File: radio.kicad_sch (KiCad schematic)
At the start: 17 parts, among them U8 Si4468/7, Y2 26MHz

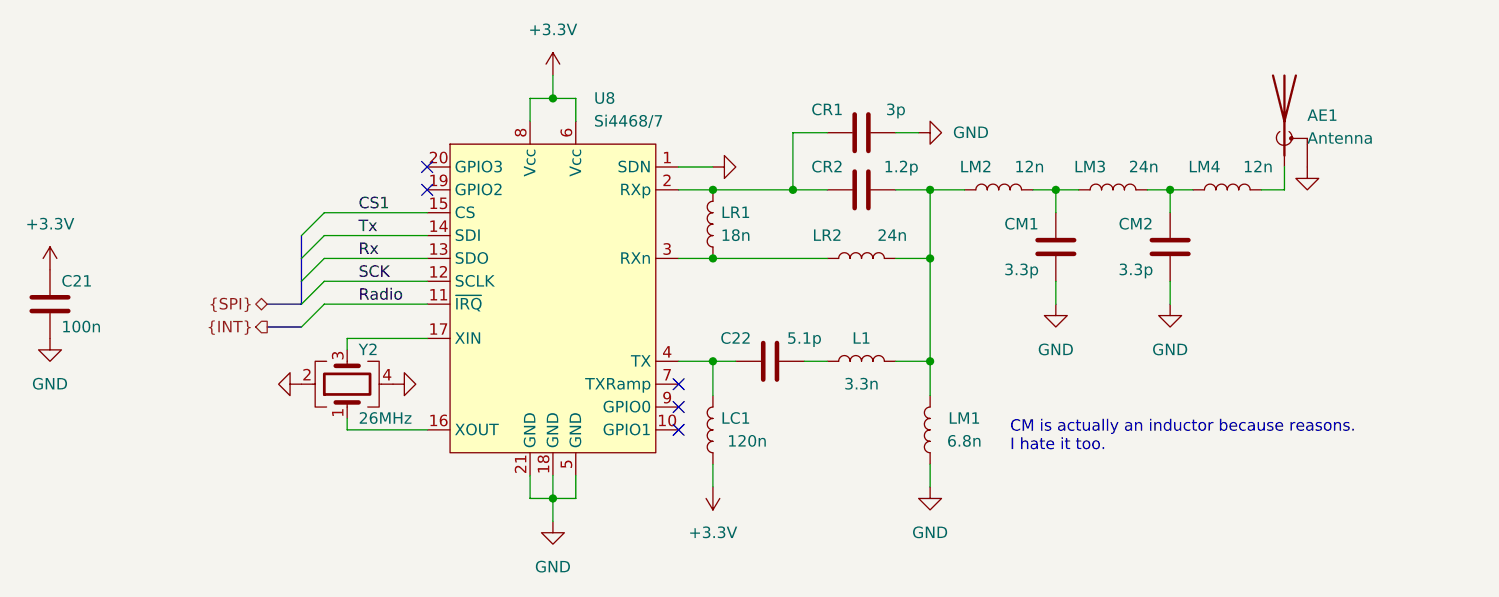
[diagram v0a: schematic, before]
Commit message: Geographical reannotated
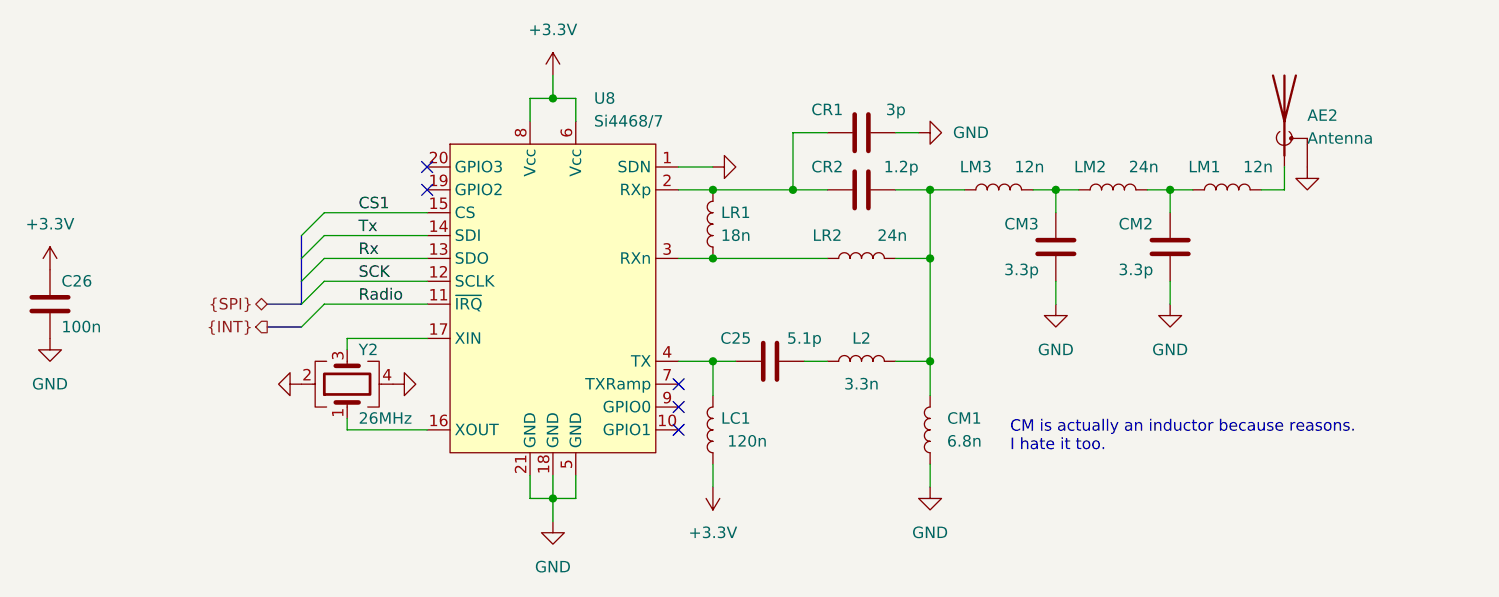
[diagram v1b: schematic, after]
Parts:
- renumbered AE1 to AE2, C22 to C25, C21 to C26, LM1 to CM1, CM1 to CM3, L1 to L2, LM4 to LM1, LM3 to LM2, LM2 to LM3
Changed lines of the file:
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@@
   (symbol (lib_id "Device:Antenna_Shield") (at 163.83 44.45 0) (unit 1)
     (in_bom yes) (on_board yes) (fields_autoplaced)
-    (property "Reference" "AE1" (id 0) (at 166.37 43.8149 0)
+    (property "Reference" "AE2" (id 0) (at 166.37 43.8149 0)
       (effects (font (size 1.27 1.27)) (justify left))
     )
@@
   (symbol (lib_id "Device:L") (at 144.78 52.07 270) (mirror x) (unit 1)
     (in_bom yes) (on_board yes)
-    (property "Reference" "LM3" (id 0) (at 142.24 49.53 90))
+    (property "Reference" "LM2" (id 0) (at 142.24 49.53 90))
     (property "Value" "24n" (id 1) (at 149.86 49.53 90)
       (effects (font (size 1.27 1.27)) (justify right))
@@
   (symbol (lib_id "Device:L") (at 116.84 71.12 90) (unit 1)
     (in_bom yes) (on_board yes)
-    (property "Reference" "L1" (id 0) (at 116.84 68.58 90))
+    (property "Reference" "L2" (id 0) (at 116.84 68.58 90))
     (property "Value" "3.3n" (id 1) (at 116.84 73.66 90))
     (property "Footprint" "Inductor_SMD:L_0603_1608Metric" (id 2) (at 116.84 71.12 0)
@@
   (symbol (lib_id "Device:L") (at 157.48 52.07 270) (mirror x) (unit 1)
     (in_bom yes) (on_board yes)
-    (property "Reference" "LM4" (id 0) (at 154.94 49.53 90))
+    (property "Reference" "LM1" (id 0) (at 154.94 49.53 90))
     (property "Value" "12n" (id 1) (at 162.56 49.53 90)
       (effects (font (size 1.27 1.27)) (justify right))
@@
   (symbol (lib_id "Device:C") (at 106.68 71.12 270) (mirror x) (unit 1)
     (in_bom yes) (on_board yes)
-    (property "Reference" "C22" (id 0) (at 102.87 68.58 90))
+    (property "Reference" "C25" (id 0) (at 102.87 68.58 90))
     (property "Value" "5.1p" (id 1) (at 110.49 68.58 90))
     (property "Footprint" "Capacitor_SMD:C_0603_1608Metric" (id 2) (at 102.87 70.1548 0)
@@
   (symbol (lib_id "Device:L") (at 124.46 78.74 180) (unit 1)
     (in_bom yes) (on_board yes)
-    (property "Reference" "LM1" (id 0) (at 128.27 77.47 0))
+    (property "Reference" "CM1" (id 0) (at 128.27 77.47 0))
     (property "Value" "6.8n" (id 1) (at 128.27 80.01 0))
     (property "Footprint" "Capacitor_SMD:C_0603_1608Metric" (id 2) (at 124.46 78.74 0)
@@
   (symbol (lib_id "Device:L") (at 132.08 52.07 270) (mirror x) (unit 1)
     (in_bom yes) (on_board yes)
-    (property "Reference" "LM2" (id 0) (at 129.54 49.53 90))
+    (property "Reference" "LM3" (id 0) (at 129.54 49.53 90))
     (property "Value" "12n" (id 1) (at 137.16 49.53 90)
       (effects (font (size 1.27 1.27)) (justify right))
@@
   (symbol (lib_id "Device:C") (at 138.43 58.42 0) (mirror y) (unit 1)
     (in_bom yes) (on_board yes)
-    (property "Reference" "CM1" (id 0) (at 134.62 55.88 0))
+    (property "Reference" "CM3" (id 0) (at 134.62 55.88 0))
     (property "Value" "3.3p" (id 1) (at 134.62 60.96 0))
     (property "Footprint" "Capacitor_SMD:C_0603_1608Metric" (id 2) (at 137.4648 62.23 0)
@@
   (symbol (lib_id "Device:C") (at 26.67 64.77 0) (unit 1)
     (in_bom yes) (on_board yes)
-    (property "Reference" "C21" (id 0) (at 27.94 62.23 0)
-      (effects (font (size 1.27 1.27)) (justify left))
-    )
+    (property "Reference" "C26" (id 0) (at 27.94 62.23 0)
+      (effects (font (size 1.27 1.27)) (justify left))
+    )

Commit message: Final refinements before issue to JLC
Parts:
- renumbered AE2 to AE1, C26 to C21, C25 to C22, CM3 to CM2, CM2 to CM3, L2 to L1, LM3 to LM1, LM1 to LM3
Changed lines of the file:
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@@
   (symbol (lib_id "Device:Antenna_Shield") (at 163.83 44.45 0) (unit 1)
     (in_bom yes) (on_board yes) (fields_autoplaced)
-    (property "Reference" "AE2" (id 0) (at 166.37 43.8149 0)
+    (property "Reference" "AE1" (id 0) (at 166.37 43.8149 0)
       (effects (font (size 1.27 1.27)) (justify left))
     )
@@
   (symbol (lib_id "power:GND") (at 100.33 49.53 90) (unit 1)
     (in_bom yes) (on_board yes) (fields_autoplaced)
-    (property "Reference" "#PWR053" (id 0) (at 106.68 49.53 0)
+    (property "Reference" "#PWR055" (id 0) (at 106.68 49.53 0)
       (effects (font (size 1.27 1.27)) hide)
     )
@@
   (symbol (lib_id "power:GND") (at 54.61 73.66 270) (unit 1)
     (in_bom yes) (on_board yes) (fields_autoplaced)
-    (property "Reference" "#PWR049" (id 0) (at 48.26 73.66 0)
+    (property "Reference" "#PWR051" (id 0) (at 48.26 73.66 0)
       (effects (font (size 1.27 1.27)) hide)
     )
@@
   (symbol (lib_id "power:GND") (at 166.37 49.53 0) (unit 1)
     (in_bom yes) (on_board yes) (fields_autoplaced)
-    (property "Reference" "#PWR059" (id 0) (at 166.37 55.88 0)
+    (property "Reference" "#PWR061" (id 0) (at 166.37 55.88 0)
       (effects (font (size 1.27 1.27)) hide)
     )
@@
   (symbol (lib_id "Device:L") (at 116.84 71.12 90) (unit 1)
     (in_bom yes) (on_board yes)
-    (property "Reference" "L2" (id 0) (at 116.84 68.58 90))
+    (property "Reference" "L1" (id 0) (at 116.84 68.58 90))
     (property "Value" "3.3n" (id 1) (at 116.84 73.66 90))
     (property "Footprint" "Inductor_SMD:L_0603_1608Metric" (id 2) (at 116.84 71.12 0)
@@
   (symbol (lib_id "power:GND") (at 151.13 64.77 0) (unit 1)
     (in_bom yes) (on_board yes) (fields_autoplaced)
-    (property "Reference" "#PWR058" (id 0) (at 151.13 71.12 0)
+    (property "Reference" "#PWR060" (id 0) (at 151.13 71.12 0)
       (effects (font (size 1.27 1.27)) hide)
     )
@@
   (symbol (lib_id "Device:L") (at 157.48 52.07 270) (mirror x) (unit 1)
     (in_bom yes) (on_board yes)
-    (property "Reference" "LM1" (id 0) (at 154.94 49.53 90))
+    (property "Reference" "LM3" (id 0) (at 154.94 49.53 90))
     (property "Value" "12n" (id 1) (at 162.56 49.53 90)
       (effects (font (size 1.27 1.27)) (justify right))
@@
   (symbol (lib_id "Device:C") (at 106.68 71.12 270) (mirror x) (unit 1)
     (in_bom yes) (on_board yes)
-    (property "Reference" "C25" (id 0) (at 102.87 68.58 90))
+    (property "Reference" "C22" (id 0) (at 102.87 68.58 90))
     (property "Value" "5.1p" (id 1) (at 110.49 68.58 90))
     (property "Footprint" "Capacitor_SMD:C_0603_1608Metric" (id 2) (at 102.87 70.1548 0)
@@
   (symbol (lib_id "power:GND") (at 64.77 73.66 90) (unit 1)
     (in_bom yes) (on_board yes) (fields_autoplaced)
-    (property "Reference" "#PWR050" (id 0) (at 71.12 73.66 0)
+    (property "Reference" "#PWR052" (id 0) (at 71.12 73.66 0)
       (effects (font (size 1.27 1.27)) hide)
     )
@@
   (symbol (lib_id "power:GND") (at 138.43 64.77 0) (unit 1)
     (in_bom yes) (on_board yes) (fields_autoplaced)
-    (property "Reference" "#PWR057" (id 0) (at 138.43 71.12 0)
+    (property "Reference" "#PWR059" (id 0) (at 138.43 71.12 0)
       (effects (font (size 1.27 1.27)) hide)
     )
@@
   (symbol (lib_id "power:+3.3V") (at 82.55 39.37 0) (unit 1)
     (in_bom yes) (on_board yes) (fields_autoplaced)
-    (property "Reference" "#PWR051" (id 0) (at 82.55 43.18 0)
+    (property "Reference" "#PWR053" (id 0) (at 82.55 43.18 0)
       (effects (font (size 1.27 1.27)) hide)
     )
@@
   (symbol (lib_id "power:GND") (at 26.67 68.58 0) (unit 1)
     (in_bom yes) (on_board yes) (fields_autoplaced)
-    (property "Reference" "#PWR048" (id 0) (at 26.67 74.93 0)
+    (property "Reference" "#PWR050" (id 0) (at 26.67 74.93 0)
       (effects (font (size 1.27 1.27)) hide)
     )
@@
   (symbol (lib_id "Device:L") (at 132.08 52.07 270) (mirror x) (unit 1)
     (in_bom yes) (on_board yes)
-    (property "Reference" "LM3" (id 0) (at 129.54 49.53 90))
+    (property "Reference" "LM1" (id 0) (at 129.54 49.53 90))
     (property "Value" "12n" (id 1) (at 137.16 49.53 90)
       (effects (font (size 1.27 1.27)) (justify right))
@@
   (symbol (lib_id "Device:C") (at 138.43 58.42 0) (mirror y) (unit 1)
     (in_bom yes) (on_board yes)
-    (property "Reference" "CM3" (id 0) (at 134.62 55.88 0))
+    (property "Reference" "CM2" (id 0) (at 134.62 55.88 0))
     (property "Value" "3.3p" (id 1) (at 134.62 60.96 0))
     (property "Footprint" "Capacitor_SMD:C_0603_1608Metric" (id 2) (at 137.4648 62.23 0)
@@
   (symbol (lib_id "power:GND") (at 123.19 45.72 90) (unit 1)
     (in_bom yes) (on_board yes) (fields_autoplaced)
-    (property "Reference" "#PWR055" (id 0) (at 129.54 45.72 0)
+    (property "Reference" "#PWR057" (id 0) (at 129.54 45.72 0)
       (effects (font (size 1.27 1.27)) hide)
     )
@@
   (symbol (lib_id "power:GND") (at 124.46 85.09 0) (unit 1)
     (in_bom yes) (on_board yes) (fields_autoplaced)
-    (property "Reference" "#PWR056" (id 0) (at 124.46 91.44 0)
+    (property "Reference" "#PWR058" (id 0) (at 124.46 91.44 0)
       (effects (font (size 1.27 1.27)) hide)
     )
@@
   (symbol (lib_id "Device:C") (at 151.13 58.42 0) (mirror y) (unit 1)
     (in_bom yes) (on_board yes)
-    (property "Reference" "CM2" (id 0) (at 147.32 55.88 0))
+    (property "Reference" "CM3" (id 0) (at 147.32 55.88 0))
     (property "Value" "3.3p" (id 1) (at 147.32 60.96 0))
     (property "Footprint" "Capacitor_SMD:C_0603_1608Metric" (id 2) (at 150.1648 62.23 0)
@@
   (symbol (lib_id "power:+3.3V") (at 100.33 85.09 180) (unit 1)
     (in_bom yes) (on_board yes) (fields_autoplaced)
-    (property "Reference" "#PWR054" (id 0) (at 100.33 81.28 0)
+    (property "Reference" "#PWR056" (id 0) (at 100.33 81.28 0)
       (effects (font (size 1.27 1.27)) hide)
     )
@@
   (symbol (lib_id "power:GND") (at 82.55 88.9 0) (unit 1)
     (in_bom yes) (on_board yes) (fields_autoplaced)
-    (property "Reference" "#PWR052" (id 0) (at 82.55 95.25 0)
+    (property "Reference" "#PWR054" (id 0) (at 82.55 95.25 0)
       (effects (font (size 1.27 1.27)) hide)
     )
@@
   (symbol (lib_id "power:+3.3V") (at 26.67 60.96 0) (unit 1)
     (in_bom yes) (on_board yes) (fields_autoplaced)
-    (property "Reference" "#PWR047" (id 0) (at 26.67 64.77 0)
+    (property "Reference" "#PWR049" (id 0) (at 26.67 64.77 0)
       (effects (font (size 1.27 1.27)) hide)
     )
@@
   (symbol (lib_id "Device:C") (at 26.67 64.77 0) (unit 1)
     (in_bom yes) (on_board yes)
-    (property "Reference" "C26" (id 0) (at 27.94 62.23 0)
-      (effects (font (size 1.27 1.27)) (justify left))
-    )
+    (property "Reference" "C21" (id 0) (at 27.94 62.23 0)
+      (effects (font (size 1.27 1.27)) (justify left))
+    )
